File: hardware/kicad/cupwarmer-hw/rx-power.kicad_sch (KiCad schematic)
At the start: 40 parts, among them J1 I2C Service, J3 STATUS_MON, U1 STWLC38JRM

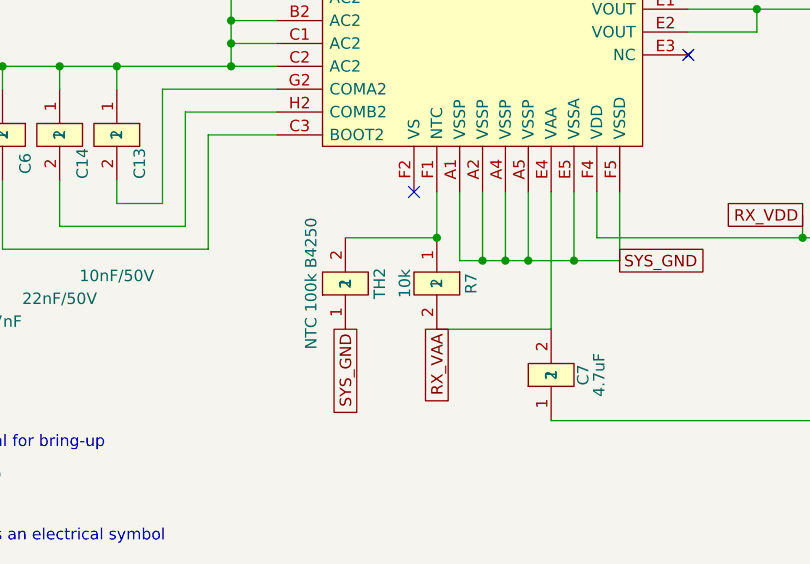
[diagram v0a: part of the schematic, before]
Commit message: Set STWLC38 NTC pull-up to 51k
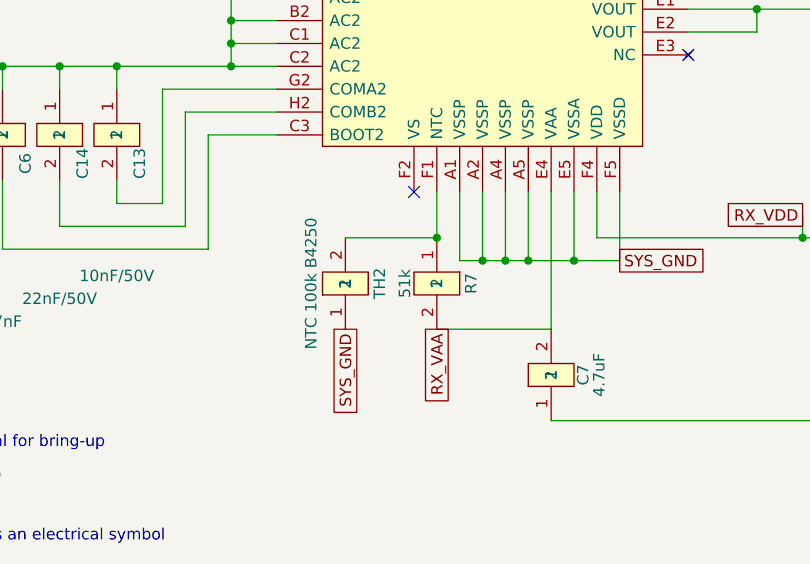
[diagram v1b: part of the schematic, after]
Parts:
- R7: value 10k -> 51k; LCSC C25804 -> C23196; MPN 0603WAF1002T5E -> 0603WAF5102T5E
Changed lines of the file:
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@@
 			)
 		)
-		(property "Value" "10k"
+		(property "Value" "51k"
 			(at 141.224 137.16 180)
 			(show_name no)
@@
 			)
 		)
-		(property "Description" "NTC pull-up to VAA (10k); forms divider with TH2 on sensors-logic sheet for IC OTP"
+		(property "Description" "NTC pull-up to VAA (51k); forms divider with 100k TH2 for STWLC38 OTP (~69C typ, VNTC,OTP=0.59V)"
 			(at 144.78 137.16 180)
 			(hide yes)
@@
 			)
 		)
-		(property "LCSC" "C25804"
+		(property "LCSC" "C23196"
 			(at 0 0 0)
 			(hide yes)
@@
 			)
 		)
-		(property "MPN" "0603WAF1002T5E"
+		(property "MPN" "0603WAF5102T5E"
 			(at 0 0 0)
 			(hide yes)

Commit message: Add parallel SOVP clamp resistors
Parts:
- added R14: RCL 200R, Resistor_SMD:R_0805_2012Metric, symbol cupwarmer:PASSIVE_2
- R4: value RCL 300R -> RCL 200R; footprint Resistor_SMD:R_0603_1608Metric -> Resistor_SMD:R_0805_2012Metric; LCSC C23025 -> C543538; MPN 0603WAF3000T5E -> ERJP06F2000V; Manufacturer UNI-ROYAL -> PANASONIC
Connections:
- net at C20.1, C21.1, C22.1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: now also R14.2
- net at R4.1, U1.A3 (IEXT): now also R14.1
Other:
- moved on the sheet: C20, C21, C22, C9, Z4

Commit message: Change power indicator LED to red
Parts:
- D1: value LED Green -> LED Red; LCSC C965804 -> C965798; MPN XL-1608UGC-04 -> XL-1608SURC-04
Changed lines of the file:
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@@
 			)
 		)
-		(property "Value" "LED Green"
+		(property "Value" "LED Red"
 			(at 233.68 124.46 0)
 			(show_name no)
@@
 			)
 		)
-		(property "LCSC" "C965804"
+		(property "LCSC" "C965798"
 			(at 7.62 0 0)
 			(hide yes)
@@
 			)
 		)
-		(property "MPN" "XL-1608UGC-04"
+		(property "MPN" "XL-1608SURC-04"
 			(at 7.62 0 0)
 			(hide yes)
